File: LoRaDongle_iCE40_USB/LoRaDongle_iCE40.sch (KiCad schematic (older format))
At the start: 7 parts

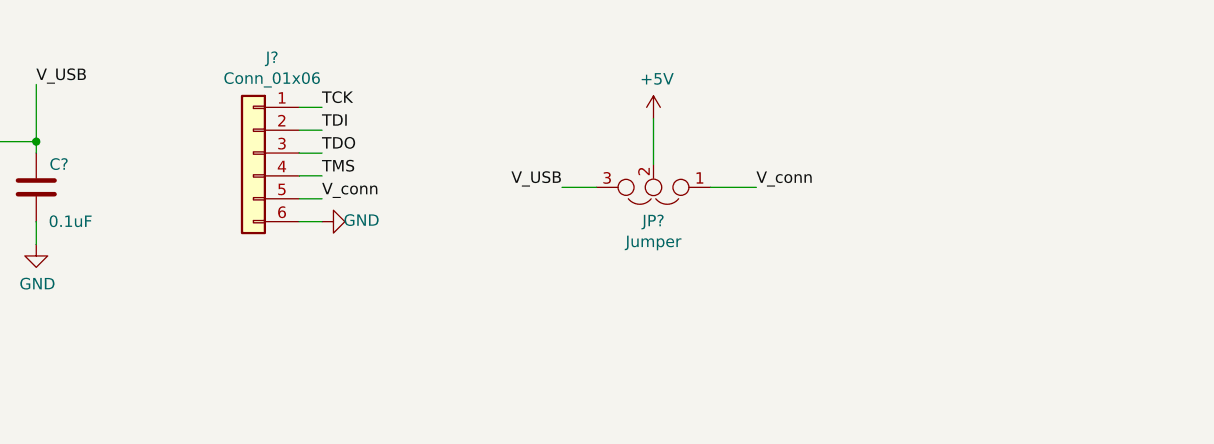
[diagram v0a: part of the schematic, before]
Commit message: initial changes to iCE40UP5k
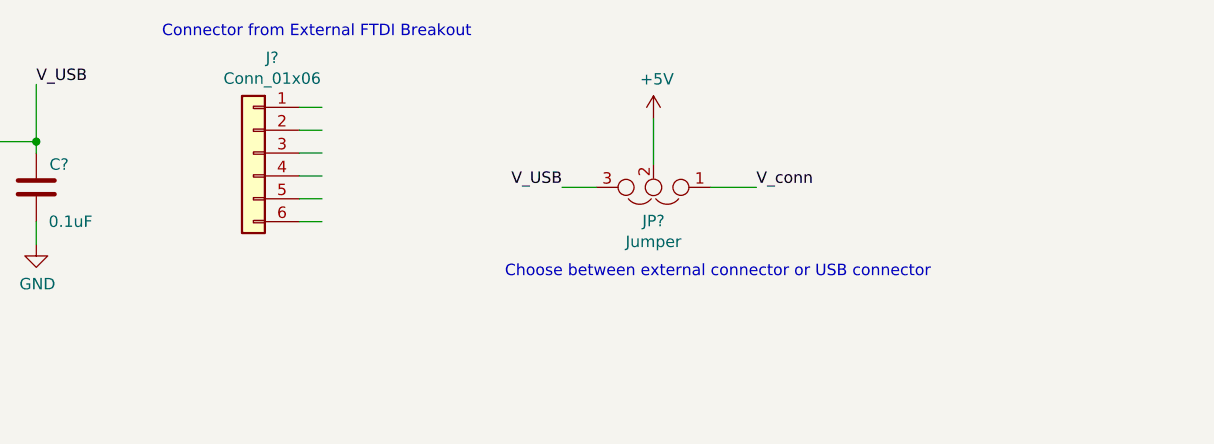
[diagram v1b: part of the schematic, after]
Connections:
- net labels removed: TCK, TDI, TDO, TMS
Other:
- note added: "Choose between external connector or USB connector"
- note added: "Connector from External FTDI Breakout"
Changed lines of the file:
@@
 	5050 1700 5150 1700
-$Comp
-L power:GND #PWR?
-U 1 1 617E7D35
-P 5150 1700
-F 0 "#PWR?" H 5150 1450 50  0001 C CNN
-F 1 "GND" V 5155 1527 50  0000 C CNN
-F 2 "" H 5150 1700 50  0001 C CNN
-F 3 "" H 5150 1700 50  0001 C CNN
-	1    5150 1700
-	0    -1   -1   0
-$EndComp
 $Comp
 L Connector_Generic:Conn_01x06 J?
@@
 Wire Wire Line
 	5050 1600 5150 1600
-Text Label 5150 1500 0    50   ~ 0
-TMS
-Text Label 5150 1400 0    50   ~ 0
-TDO
-Text Label 5150 1300 0    50   ~ 0
-TDI
-Text Label 5150 1200 0    50   ~ 0
-TCK
 Wire Wire Line
 	3900 1700 3900 1800
@@
 	-1   0    0    1
 $EndComp
-Text Label 5150 1600 0    50   ~ 0
-V_conn
 Text Label 7050 1550 0    50   ~ 0
 V_conn
@@
 F3 "DM" I L 3150 3950 50
 $EndSheet
+Text Notes 4450 900  0    50   ~ 0
+Connector from External FTDI Breakout
+Text Notes 5950 1950 0    50   ~ 0
+Choose between external connector or USB connector
 $EndSCHEMATC

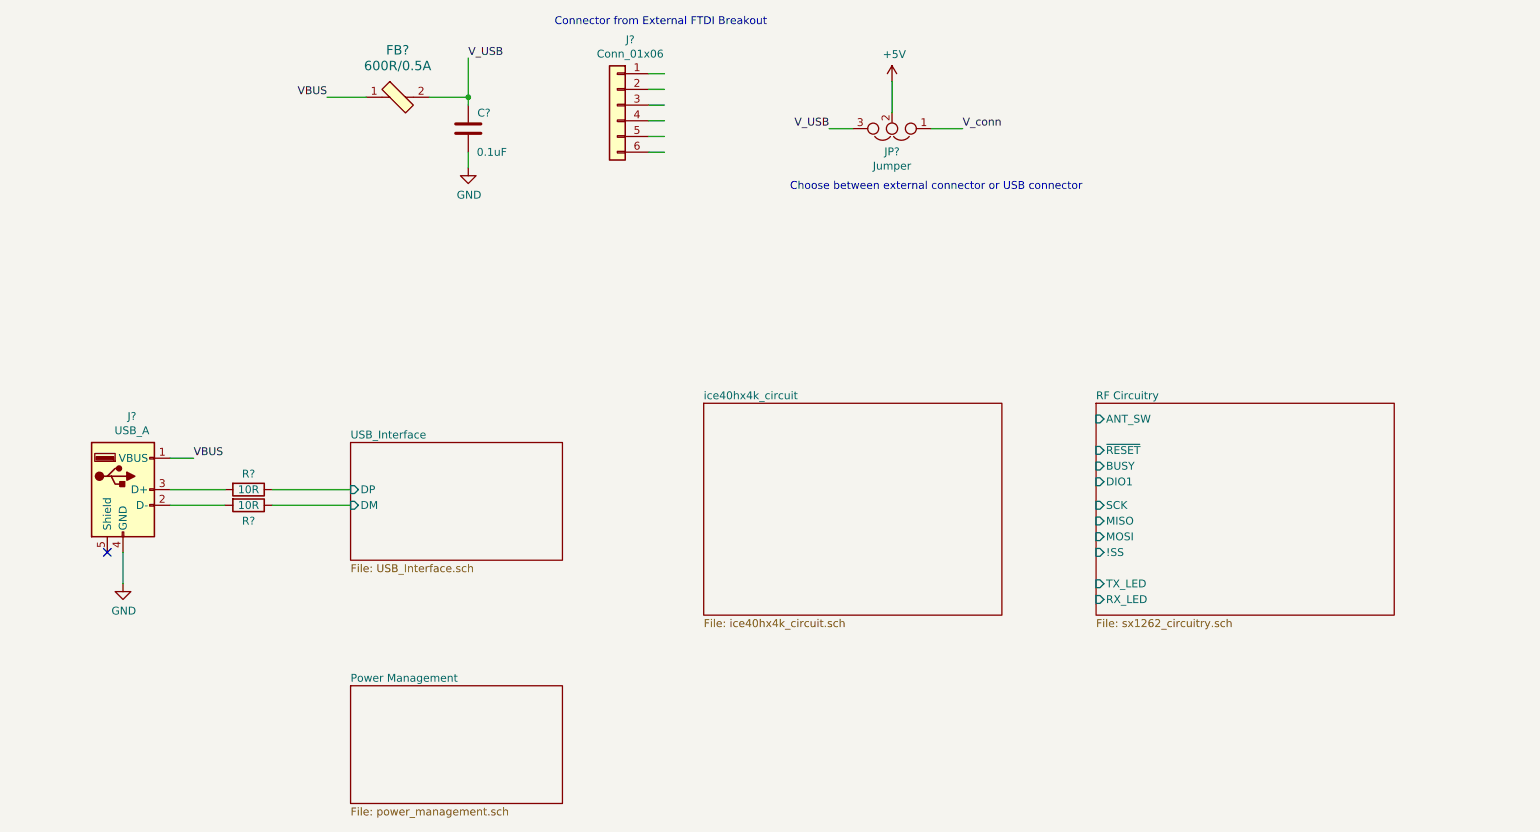
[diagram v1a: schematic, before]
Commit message: changed to sx1261
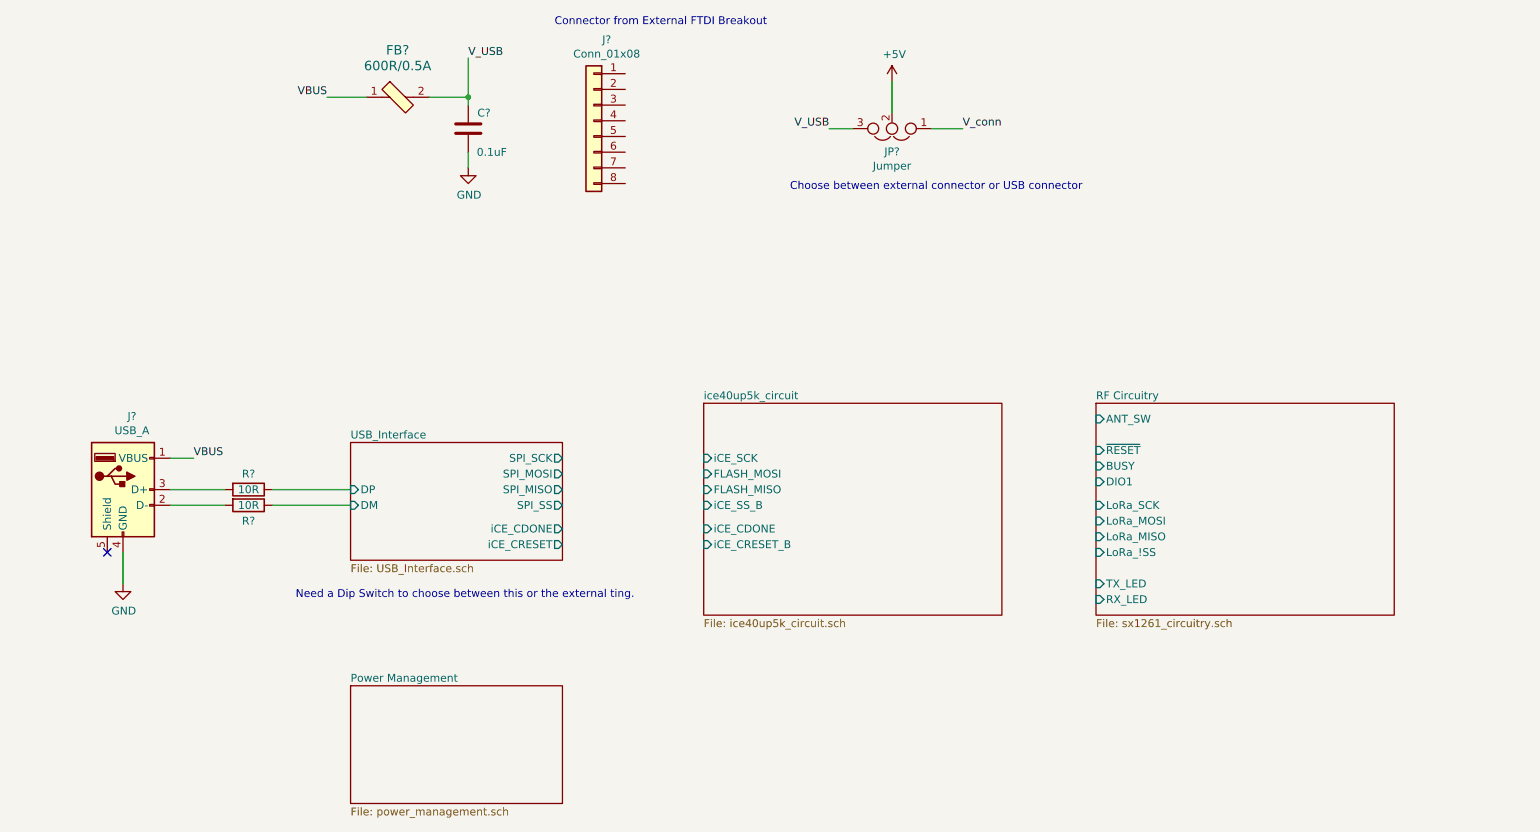
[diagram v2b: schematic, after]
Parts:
- removed J?: Conn_01x06, symbol Connector_Generic:Conn_01x06
- added J?: Conn_01x08, Connector_PinHeader_1.00mm:PinHeader_1x08_P1.00mm_Vertical, symbol Connector_Generic:Conn_01x08
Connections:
- wire segments 20 -> 14
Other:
- note added: "Need a Dip Switch to choose between this or the external ting."
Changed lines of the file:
@@
 $EndComp
-Wire Wire Line
-	5050 1700 5150 1700
-$Comp
-L Connector_Generic:Conn_01x06 J?
-U 1 1 617E562D
-P 4850 1400
-F 0 "J?" H 4768 1817 50  0000 C CNN
-F 1 "Conn_01x06" H 4768 1726 50  0000 C CNN
-F 2 "" H 4850 1400 50  0001 C CNN
-F 3 "~" H 4850 1400 50  0001 C CNN
-	1    4850 1400
-	-1   0    0    -1
-$EndComp
-Wire Wire Line
-	5050 1600 5150 1600
 Wire Wire Line
 	3900 1700 3900 1800
@@
 	1    0    0    -1
 $EndComp
-$Sheet
-S 7900 3300 1900 1350
-U 614F0720
-F0 "RF Circuitry" 50
-F1 "sx1262_circuitry.sch" 50
-F2 "SCK" I L 7900 3950 50
-F3 "MISO" I L 7900 4050 50
-F4 "MOSI" I L 7900 4150 50
-F5 "!SS" I L 7900 4250 50
-F6 "ANT_SW" I L 7900 3400 50
-F7 "~RESET" I L 7900 3600 50
-F8 "BUSY" I L 7900 3700 50
-F9 "DIO1" I L 7900 3800 50
-F10 "TX_LED" I L 7900 4450 50
-F11 "RX_LED" I L 7900 4550 50
-$EndSheet
-Wire Wire Line
-	5050 1200 5150 1200
-Wire Wire Line
-	5050 1300 5150 1300
-Wire Wire Line
-	5050 1400 5150 1400
-Wire Wire Line
-	5050 1500 5150 1500
 $Comp
 L Device:Jumper_NC_Dual JP?
@@
 	2000 3850 2350 3850
 $Sheet
-S 5400 3300 1900 1350
-U 618D30E5
-F0 "ice40hx4k_circuit" 50
-F1 "ice40hx4k_circuit.sch" 50
-$EndSheet
-$Sheet
 S 3150 3550 1350 750
 U 618AACD4
@@
 F2 "DP" I L 3150 3850 50
 F3 "DM" I L 3150 3950 50
+F4 "SPI_SCK" O R 4500 3650 50
+F5 "SPI_MOSI" O R 4500 3750 50
+F6 "SPI_MISO" O R 4500 3850 50
+F7 "SPI_SS" O R 4500 3950 50
+F8 "iCE_CDONE" O R 4500 4100 50
+F9 "iCE_CRESET" O R 4500 4200 50
 $EndSheet
 Text Notes 4450 900  0    50   ~ 0
@@
 Text Notes 5950 1950 0    50   ~ 0
 Choose between external connector or USB connector
+$Sheet
+S 5400 3300 1900 1350
+U 618D30E5
+F0 "ice40up5k_circuit" 50
+F1 "ice40up5k_circuit.sch" 50
+F2 "iCE_CDONE" I L 5400 4100 50
+F3 "iCE_CRESET_B" I L 5400 4200 50
+F4 "iCE_SCK" I L 5400 3650 50
+F5 "iCE_SS_B" I L 5400 3950 50
+F6 "FLASH_MOSI" I L 5400 3750 50
+F7 "FLASH_MISO" I L 5400 3850 50
+$EndSheet
+Text Notes 2800 4550 0    50   ~ 0
+Need a Dip Switch to choose between this or the external ting.
+$Comp
+L Connector_Generic:Conn_01x08 J?
+U 1 1 61B8EE64
+P 4700 1500
+F 0 "J?" H 4618 2017 50  0000 C CNN
+F 1 "Conn_01x08" H 4618 1926 50  0000 C CNN
+F 2 "Connector_PinHeader_1.00mm:PinHeader_1x08_P1.00mm_Vertical" H 4700 1500 50  0001 C CNN
+F 3 "~" H 4700 1500 50  0001 C CNN
+	1    4700 1500
+	-1   0    0    -1
+$EndComp
+$Sheet
+S 7900 3300 1900 1350
+U 614F0720
+F0 "RF Circuitry" 50
+F1 "sx1261_circuitry.sch" 50
+F2 "ANT_SW" I L 7900 3400 50
+F3 "~RESET" I L 7900 3600 50
+F4 "BUSY" I L 7900 3700 50
+F5 "DIO1" I L 7900 3800 50
+F6 "TX_LED" I L 7900 4450 50
+F7 "RX_LED" I L 7900 4550 50
+F8 "LoRa_!SS" I L 7900 4250 50
+F9 "LoRa_MISO" I L 7900 4150 50
+F10 "LoRa_MOSI" I L 7900 4050 50
+F11 "LoRa_SCK" I L 7900 3950 50
+$EndSheet
 $EndSCHEMATC

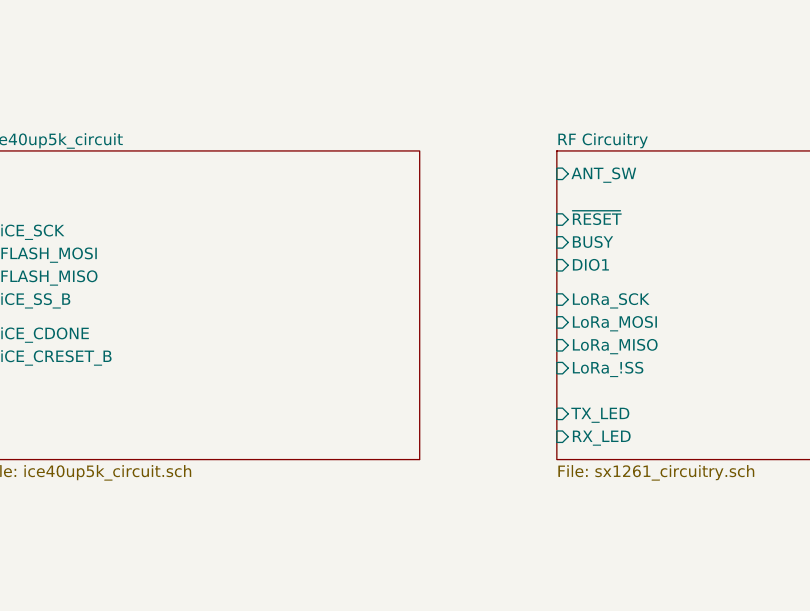
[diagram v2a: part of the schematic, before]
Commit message: connected FPGA to SX1261
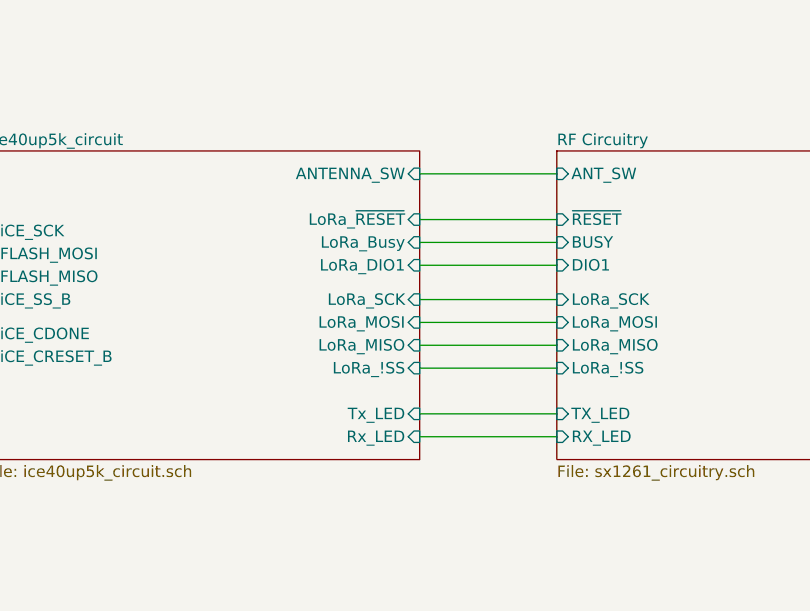
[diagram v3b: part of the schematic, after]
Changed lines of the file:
@@
 F6 "FLASH_MOSI" I L 5400 3750 50
 F7 "FLASH_MISO" I L 5400 3850 50
+F8 "Tx_LED" I R 7300 4450 50
+F9 "Rx_LED" I R 7300 4550 50
+F10 "ANTENNA_SW" I R 7300 3400 50
+F11 "LoRa_~RESET" I R 7300 3600 50
+F12 "LoRa_Busy" I R 7300 3700 50
+F13 "LoRa_DIO1" I R 7300 3800 50
+F14 "LoRa_SCK" I R 7300 3950 50
+F15 "LoRa_MOSI" I R 7300 4050 50
+F16 "LoRa_MISO" I R 7300 4150 50
+F17 "LoRa_!SS" I R 7300 4250 50
 $EndSheet
 Text Notes 2800 4550 0    50   ~ 0
@@
 F11 "LoRa_SCK" I L 7900 3950 50
 $EndSheet
+Wire Wire Line
+	7300 3400 7900 3400
+Wire Wire Line
+	7300 3600 7900 3600
+Wire Wire Line
+	7300 3700 7900 3700
+Wire Wire Line
+	7300 3800 7900 3800
+Wire Wire Line
+	7300 3950 7900 3950
+Wire Wire Line
+	7300 4050 7900 4050
+Wire Wire Line
+	7300 4150 7900 4150
+Wire Wire Line
+	7300 4250 7900 4250
+Wire Wire Line
+	7300 4450 7900 4450
+Wire Wire Line
+	7300 4550 7900 4550
 $EndSCHEMATC

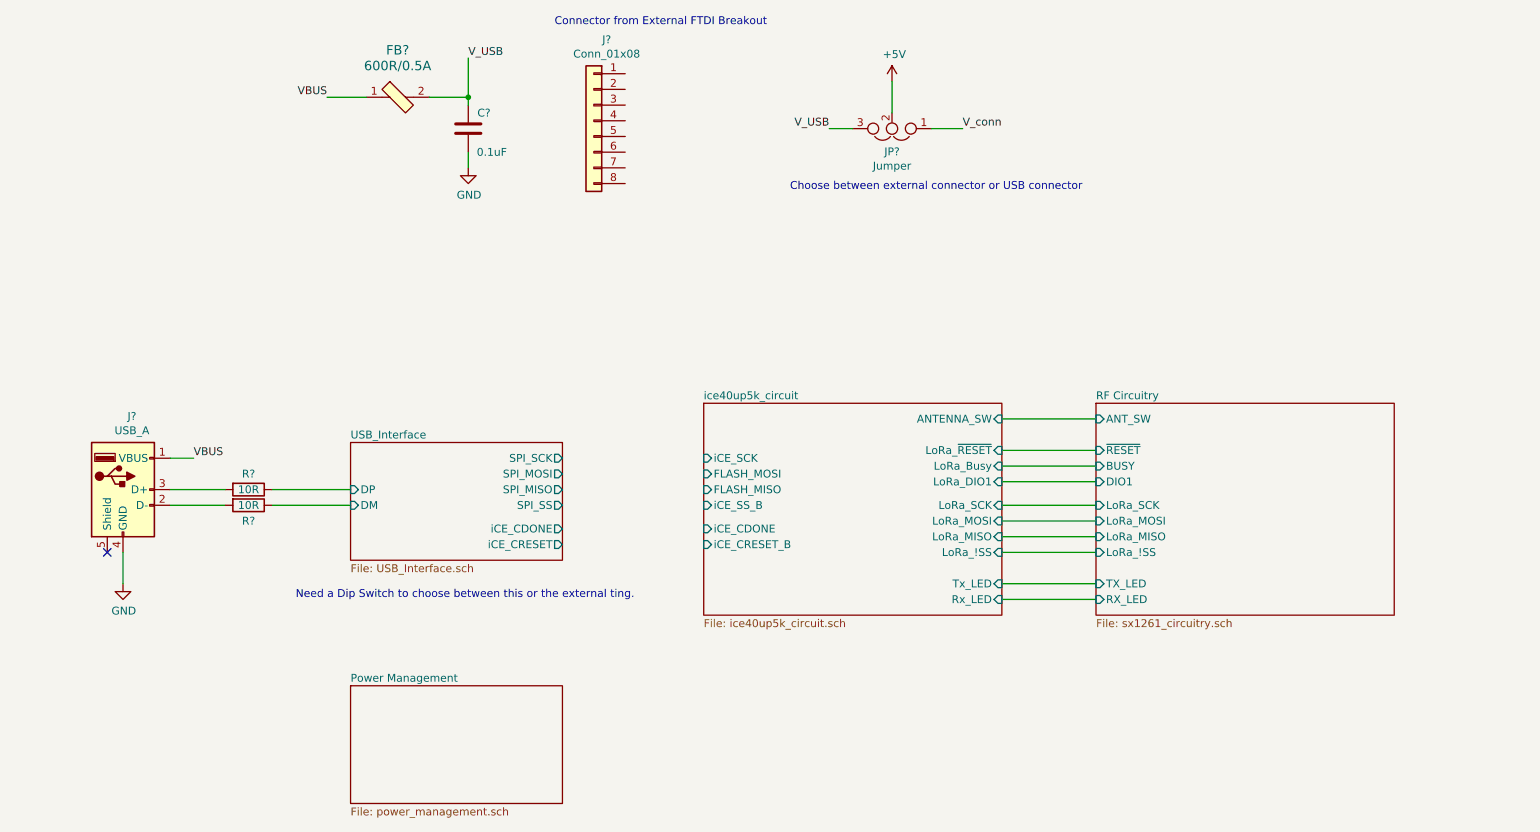
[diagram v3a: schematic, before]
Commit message: added footprints
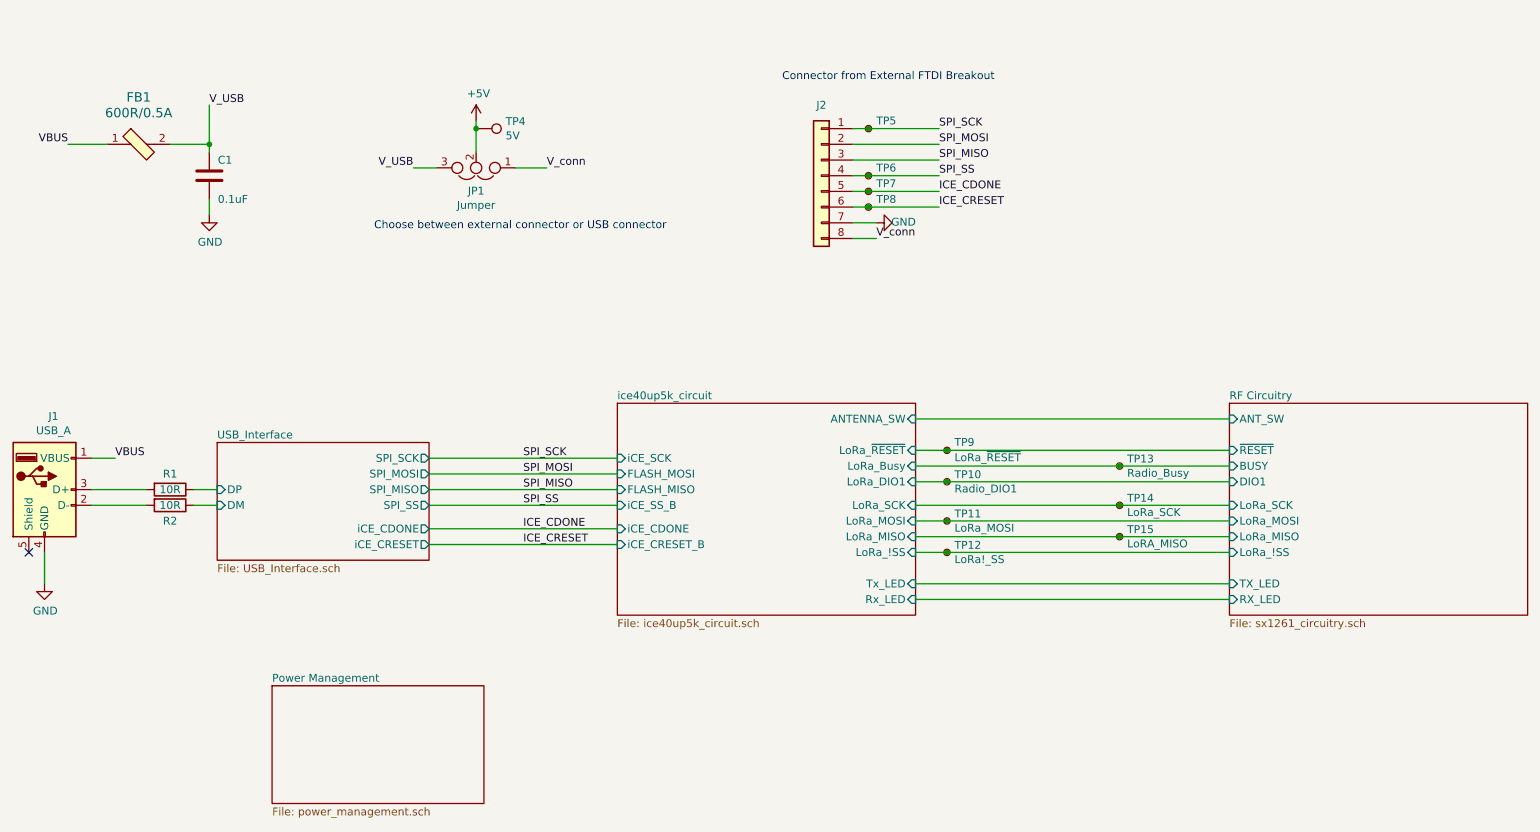
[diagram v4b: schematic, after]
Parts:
- added TP10: Radio_DIO1, TestPoint:TestPoint_Pad_D2.5mm, symbol Connector:TestPoint_Small
- added TP11: LoRa_MOSI, TestPoint:TestPoint_Pad_D2.5mm, symbol Connector:TestPoint_Small
- added TP12: LoRa!_SS, TestPoint:TestPoint_Pad_D2.5mm, symbol Connector:TestPoint_Small
- added TP13: Radio_Busy, TestPoint:TestPoint_Pad_D2.5mm, symbol Connector:TestPoint_Small
- added TP14: LoRa_SCK, TestPoint:TestPoint_Pad_D2.5mm, symbol Connector:TestPoint_Small
- added TP15: LoRA_MISO, TestPoint:TestPoint_Pad_D2.5mm, symbol Connector:TestPoint_Small
- added TP4: 5V, TestPoint:TestPoint_Pad_D2.5mm, symbol Connector:TestPoint
- added TP5: iCE_SCK, TestPoint:TestPoint_Pad_D2.5mm, symbol Connector:TestPoint_Small
- added TP6: iCE_SS_B, TestPoint:TestPoint_Pad_D2.5mm, symbol Connector:TestPoint_Small
- added TP7: iCE_CDONE, TestPoint:TestPoint_Pad_D2.5mm, symbol Connector:TestPoint_Small
- added TP8: iCE_CRESET, TestPoint:TestPoint_Pad_D2.5mm, symbol Connector:TestPoint_Small
- added TP9: LoRa_~RESET, TestPoint:TestPoint_Pad_D2.5mm, symbol Connector:TestPoint_Small
- J2: renamed from J?; footprint Connector_PinHeader_1.00mm:PinHeader_1x08_P1.00mm_Vertical -> Connector_PinHeader_2.54mm:PinHeader_2x04_P2.54mm_Vertical
- JP1: renamed from JP?; footprint (none) -> Connector_PinHeader_2.54mm:PinHeader_1x03_P2.54mm_Vertical
- R1, R2: renamed from R?; footprint (none) -> Resistor_SMD:R_0402_1005Metric
- gave numbers to parts that had none: 3
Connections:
- net +5V: now also TP4.1
- net GND: now also J2.7 (Pin_7)
- net RF Circuitry/BUSY: now also TP13.1
- net RF Circuitry/DIO1: now also TP10.1
- net RF Circuitry/LoRa_!SS: now also TP12.1
- net RF Circuitry/LoRa_MISO: now also TP15.1
- net RF Circuitry/LoRa_MOSI: now also TP11.1
- net RF Circuitry/LoRa_SCK: now also TP14.1
- net RF Circuitry/~RESET: now also TP9.1
- net V_conn: now also J2.8 (Pin_8)
- net SPI_SCK: now reaches J2.1 (Pin_1)
- net SPI_SCK: now also TP5.1
- net SPI_MOSI: now reaches J2.2 (Pin_2)
- net SPI_MISO: now reaches J2.3 (Pin_3)
- net SPI_SS: now reaches J2.4 (Pin_4)
- net SPI_SS: now also TP6.1
- net ICE_CDONE: now reaches J2.5 (Pin_5)
- net ICE_CDONE: now also TP7.1
- net ICE_CRESET: now reaches J2.6 (Pin_6)
- net ICE_CRESET: now also TP8.1
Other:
- note removed: "Need a Dip Switch to choose between this or the external ting."
- moved on the sheet: C1, FB1, J1, J2, JP1, R1, R2
